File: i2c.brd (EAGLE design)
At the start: 36.5 x 34.3 mm, 7 parts, among them IC1 24LC024SN, IC2 24LC024ST, X1 2510-

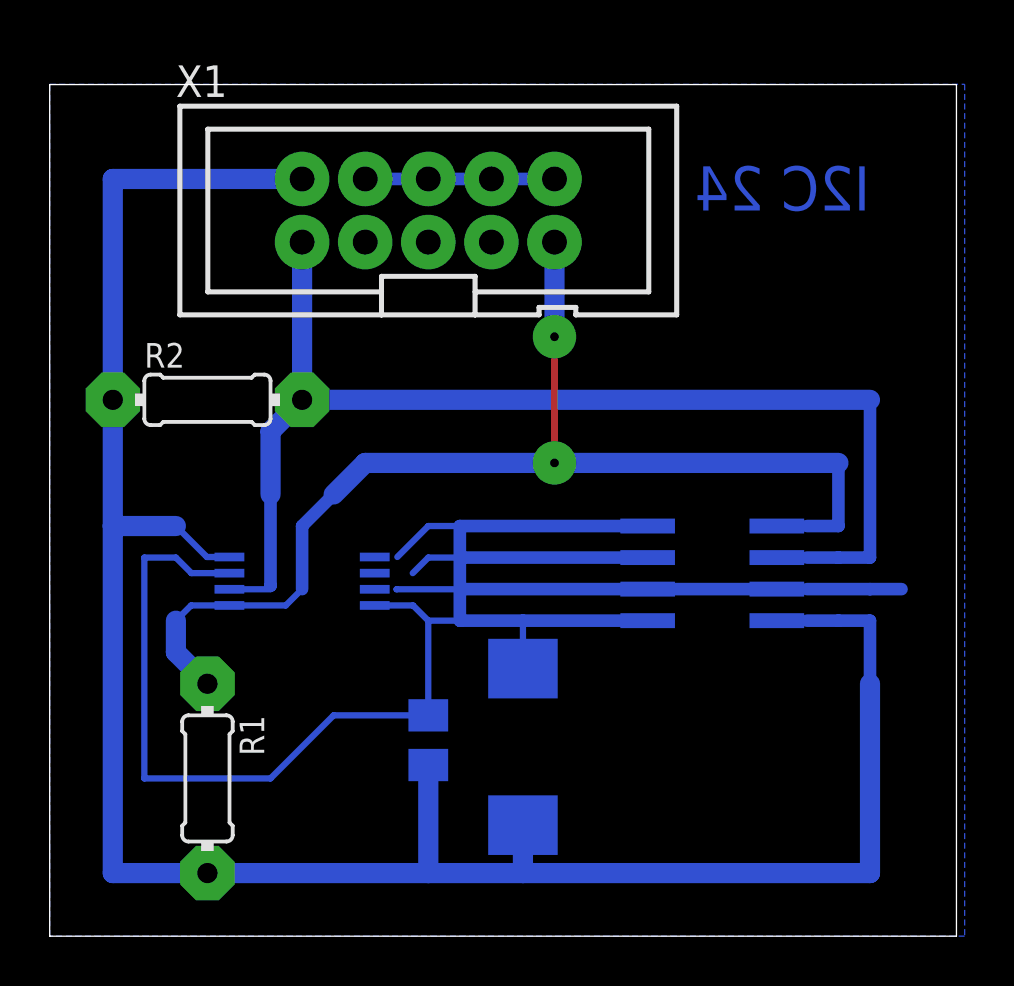
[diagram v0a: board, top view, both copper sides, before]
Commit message: Подправлены дорожки
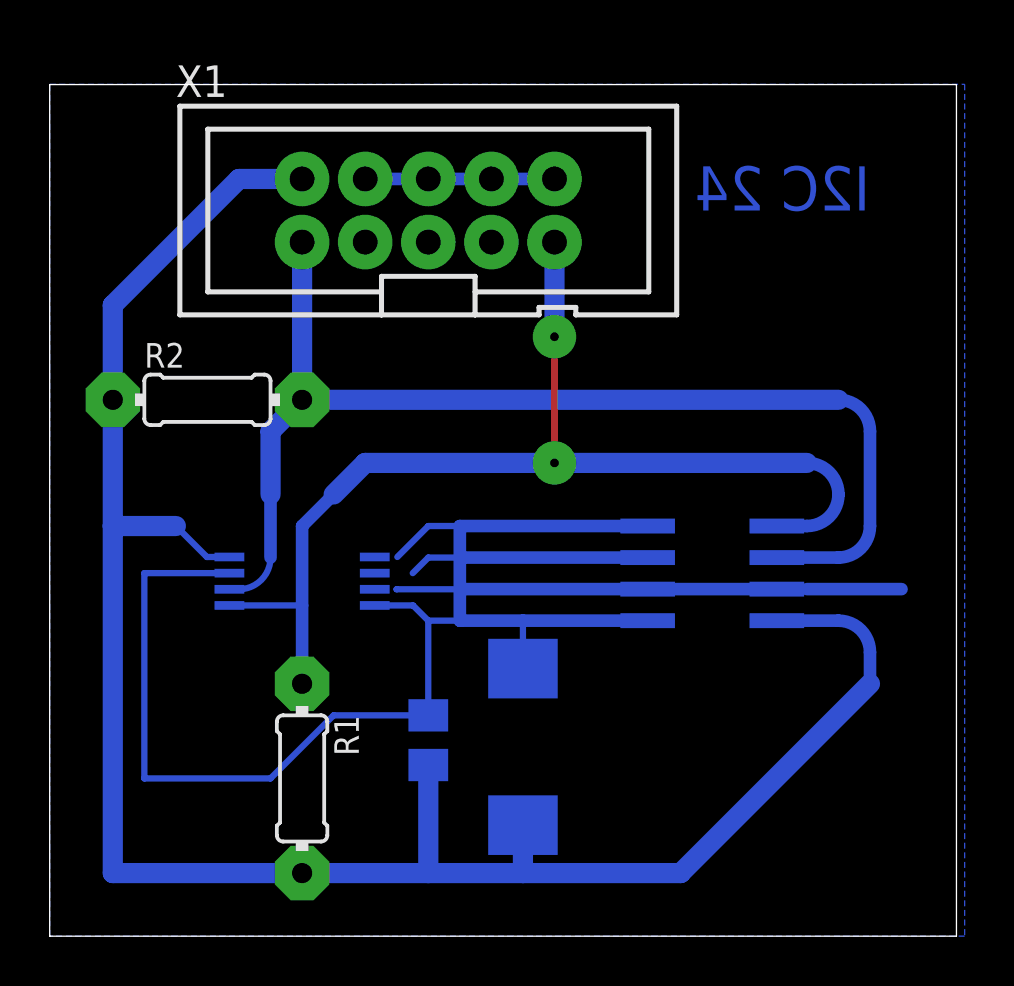
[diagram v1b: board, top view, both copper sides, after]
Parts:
- moved R1 3.81 mm to (31.8, 36.8)
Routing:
- net VCC: track 91.4 -> 84.5 mm
- net MISO: track 49.7 -> 44.6 mm
- net GND: track 94.1 -> 93.3 mm
- net MOSI: track 49.0 -> 48.1 mm

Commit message: Увеличено расстояние до заливки
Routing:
- net GND: track 93.3 -> 74.3 mm
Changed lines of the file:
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@@
 <grid distance="1.27" unitdist="mm" unit="mm" style="lines" multiple="1" display="yes" altdistance="5" altunitdist="mil" altunit="mm"/>
 <layers>
-<layer number="1" name="Top" color="4" fill="1" visible="yes" active="yes"/>
+<layer number="1" name="Top" color="4" fill="1" visible="no" active="yes"/>
 <layer number="16" name="Bottom" color="1" fill="1" visible="yes" active="yes"/>
 <layer number="17" name="Pads" color="2" fill="1" visible="yes" active="yes"/>
 <layer number="18" name="Vias" color="2" fill="1" visible="yes" active="yes"/>
-<layer number="19" name="Unrouted" color="6" fill="1" visible="yes" active="yes"/>
+<layer number="19" name="Unrouted" color="6" fill="1" visible="no" active="yes"/>
 <layer number="20" name="Dimension" color="24" fill="1" visible="yes" active="yes"/>
-<layer number="21" name="tPlace" color="7" fill="1" visible="yes" active="yes"/>
-<layer number="22" name="bPlace" color="7" fill="1" visible="yes" active="yes"/>
-<layer number="23" name="tOrigins" color="15" fill="1" visible="yes" active="yes"/>
-<layer number="24" name="bOrigins" color="15" fill="1" visible="yes" active="yes"/>
-<layer number="25" name="tNames" color="7" fill="1" visible="yes" active="yes"/>
-<layer number="26" name="bNames" color="7" fill="1" visible="yes" active="yes"/>
-<layer number="27" name="tValues" color="7" fill="1" visible="yes" active="yes"/>
-<layer number="28" name="bValues" color="7" fill="1" visible="yes" active="yes"/>
-<layer number="29" name="tStop" color="7" fill="3" visible="yes" active="yes"/>
-<layer number="30" name="bStop" color="7" fill="6" visible="yes" active="yes"/>
-<layer number="31" name="tCream" color="7" fill="4" visible="yes" active="yes"/>
-<layer number="32" name="bCream" color="7" fill="5" visible="yes" active="yes"/>
-<layer number="33" name="tFinish" color="6" fill="3" visible="yes" active="yes"/>
-<layer number="34" name="bFinish" color="6" fill="6" visible="yes" active="yes"/>
-<layer number="35" name="tGlue" color="7" fill="4" visible="yes" active="yes"/>
-<layer number="36" name="bGlue" color="7" fill="5" visible="yes" active="yes"/>
-<layer number="37" name="tTest" color="7" fill="1" visible="yes" active="yes"/>
-<layer number="38" name="bTest" color="7" fill="1" visible="yes" active="yes"/>
-<layer number="39" name="tKeepout" color="4" fill="11" visible="yes" active="yes"/>
-<layer number="40" name="bKeepout" color="1" fill="11" visible="yes" active="yes"/>
-<layer number="41" name="tRestrict" color="4" fill="10" visible="yes" active="yes"/>
+<layer number="21" name="tPlace" color="7" fill="1" visible="no" active="yes"/>
+<layer number="22" name="bPlace" color="7" fill="1" visible="no" active="yes"/>
+<layer number="23" name="tOrigins" color="15" fill="1" visible="no" active="yes"/>
+<layer number="24" name="bOrigins" color="15" fill="1" visible="no" active="yes"/>
+<layer number="25" name="tNames" color="7" fill="1" visible="no" active="yes"/>
+<layer number="26" name="bNames" color="7" fill="1" visible="no" active="yes"/>
+<layer number="27" name="tValues" color="7" fill="1" visible="no" active="yes"/>
+<layer number="28" name="bValues" color="7" fill="1" visible="no" active="yes"/>
+<layer number="29" name="tStop" color="7" fill="3" visible="no" active="yes"/>
+<layer number="30" name="bStop" color="7" fill="6" visible="no" active="yes"/>
+<layer number="31" name="tCream" color="7" fill="4" visible="no" active="yes"/>
+<layer number="32" name="bCream" color="7" fill="5" visible="no" active="yes"/>
+<layer number="33" name="tFinish" color="6" fill="3" visible="no" active="yes"/>
+<layer number="34" name="bFinish" color="6" fill="6" visible="no" active="yes"/>
+<layer number="35" name="tGlue" color="7" fill="4" visible="no" active="yes"/>
+<layer number="36" name="bGlue" color="7" fill="5" visible="no" active="yes"/>
+<layer number="37" name="tTest" color="7" fill="1" visible="no" active="yes"/>
+<layer number="38" name="bTest" color="7" fill="1" visible="no" active="yes"/>
+<layer number="39" name="tKeepout" color="4" fill="11" visible="no" active="yes"/>
+<layer number="40" name="bKeepout" color="1" fill="11" visible="no" active="yes"/>
+<layer number="41" name="tRestrict" color="4" fill="10" visible="no" active="yes"/>
 <layer number="42" name="bRestrict" color="1" fill="10" visible="yes" active="yes"/>
-<layer number="43" name="vRestrict" color="2" fill="10" visible="yes" active="yes"/>
-<layer number="44" name="Drills" color="7" fill="1" visible="yes" active="yes"/>
-<layer number="45" name="Holes" color="7" fill="1" visible="yes" active="yes"/>
-<layer number="46" name="Milling" color="3" fill="1" visible="yes" active="yes"/>
-<layer number="47" name="Measures" color="7" fill="1" visible="yes" active="yes"/>
-<layer number="48" name="Document" color="7" fill="1" visible="yes" active="yes"/>
-<layer number="49" name="Reference" color="7" fill="1" visible="yes" active="yes"/>
-<layer number="51" name="tDocu" color="7" fill="1" visible="yes" active="yes"/>
-<layer number="52" name="bDocu" color="7" fill="1" visible="yes" active="yes"/>
+<layer number="43" name="vRestrict" color="2" fill="10" visible="no" active="yes"/>
+<layer number="44" name="Drills" color="7" fill="1" visible="no" active="yes"/>
+<layer number="45" name="Holes" color="7" fill="1" visible="no" active="yes"/>
+<layer number="46" name="Milling" color="3" fill="1" visible="no" active="yes"/>
+<layer number="47" name="Measures" color="7" fill="1" visible="no" active="yes"/>
+<layer number="48" name="Document" color="7" fill="1" visible="no" active="yes"/>
+<layer number="49" name="Reference" color="7" fill="1" visible="no" active="yes"/>
+<layer number="51" name="tDocu" color="7" fill="1" visible="no" active="yes"/>
+<layer number="52" name="bDocu" color="7" fill="1" visible="no" active="yes"/>
 <layer number="88" name="SimResults" color="9" fill="1" visible="no" active="no"/>
 <layer number="89" name="SimProbes" color="9" fill="1" visible="no" active="no"/>
@@
 <wire x1="21.59" y1="64.76" x2="21.59" y2="30.48" width="0" layer="20"/>
 <polygon width="0.2" layer="42">
-<vertex x="33.02" y="39.37"/>
+<vertex x="33.02" y="38.1"/>
 <vertex x="33.02" y="30.48"/>
 <vertex x="58.42" y="30.48"/>
-<vertex x="58.42" y="39.37"/>
+<vertex x="58.42" y="38.1"/>
 </polygon>
 <polygon width="0.2" layer="42">
@@
 </polygon>
 <polygon width="0.2" layer="42">
-<vertex x="33.02" y="49.53"/>
-<vertex x="33.02" y="48.26"/>
+<vertex x="48.26" y="49.53"/>
+<vertex x="48.26" y="48.26"/>
 <vertex x="53.34" y="48.26"/>
 <vertex x="53.34" y="49.53"/>
@@
 <vertex x="48.26" y="48.26"/>
 <vertex x="54.61" y="48.26"/>
-<vertex x="54.61" y="39.37"/>
-<vertex x="48.26" y="39.37"/>
+<vertex x="54.61" y="38.1"/>
+<vertex x="48.26" y="38.1"/>
 </polygon>
 <polygon width="0.2" layer="42">
@@
 </polygon>
 <text x="54.61" y="59.69" size="1.778" layer="16" rot="MR0">I2C 24</text>
-<polygon width="0.2" layer="42">
-<vertex x="33.909" y="47.244"/>
-<vertex x="35.306" y="47.244"/>
-<vertex x="34.6075" y="46.5455"/>
-</polygon>
-<polygon width="0.2" layer="42">
-<vertex x="44.958" y="41.402"/>
-<vertex x="45.72" y="42.164"/>
-<vertex x="46.482" y="41.402"/>
-</polygon>
 <polygon width="0.2" layer="42">
 <vertex x="26.67" y="45.72"/>
@@
 <wire x1="28.825" y1="45.0935" x2="25.4" y2="45.0935" width="0.254" layer="16"/>
 <wire x1="50.86" y1="44.45" x2="45.66" y2="44.45" width="0.508" layer="16"/>
-<wire x1="25.4" y1="45.0935" x2="25.4" y2="36.83" width="0.254" layer="16"/>
-<wire x1="36.83" y1="39.37" x2="33.02" y2="39.37" width="0.254" layer="16"/>
-<wire x1="33.02" y1="39.37" x2="30.48" y2="36.83" width="0.254" layer="16"/>
-<wire x1="30.48" y1="36.83" x2="25.4" y2="36.83" width="0.254" layer="16"/>
 <wire x1="36.83" y1="39.37" x2="36.83" y2="43.18" width="0.254" layer="16"/>
 <wire x1="40.64" y1="41.25" x2="40.64" y2="43.18" width="0.254" layer="16"/>
@@
 <wire x1="36.83" y1="60.96" x2="39.37" y2="60.96" width="0.508" layer="16"/>
 <wire x1="34.29" y1="60.96" x2="36.83" y2="60.96" width="0.508" layer="16"/>
-<polygon width="0.254" layer="16">
+<polygon width="0.254" layer="16" isolate="0.4064">
 <vertex x="21.59" y="64.77"/>
 <vertex x="58.42" y="64.77"/>
@@
 <vertex x="21.59" y="30.48"/>
 </polygon>
-<wire x1="52.07" y1="44.45" x2="55.88" y2="44.45" width="0.508" layer="16"/>
-<wire x1="38.0765" y1="47.0135" x2="36.83" y2="60.96" width="0" layer="19" extent="16-16"/>
+<wire x1="50.86" y1="44.45" x2="54.61" y2="44.45" width="0.508" layer="16"/>
+<wire x1="54.61" y1="44.45" x2="55.88" y2="45.72" width="0.508" layer="16" curve="90"/>
 </signal>
 <signal name="RST">
